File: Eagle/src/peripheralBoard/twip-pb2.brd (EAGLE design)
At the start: 110.2 x 69.8 mm, 31 parts, among them J1 UJ2-BH-1-TH, Q2 IRFD9120

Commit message: Update twip-pb2.brd
 mosfet pullup changes
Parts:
- moved R1 2.54 mm to (30.5, 73.7), turned to 285 degrees
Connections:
- net N$26: now also R1.2; no longer R1.1
- net N$7: now also R1.1; no longer R1.2
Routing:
- net N$8: track 137.1 -> 135.8 mm
- net N$26: track 24.2 -> 25.3 mm
- net N$11: track 28.9 -> 27.9 mm
- net N$18: track 29.1 -> 28.4 mm
- net N$19: track 29.4 -> 28.8 mm

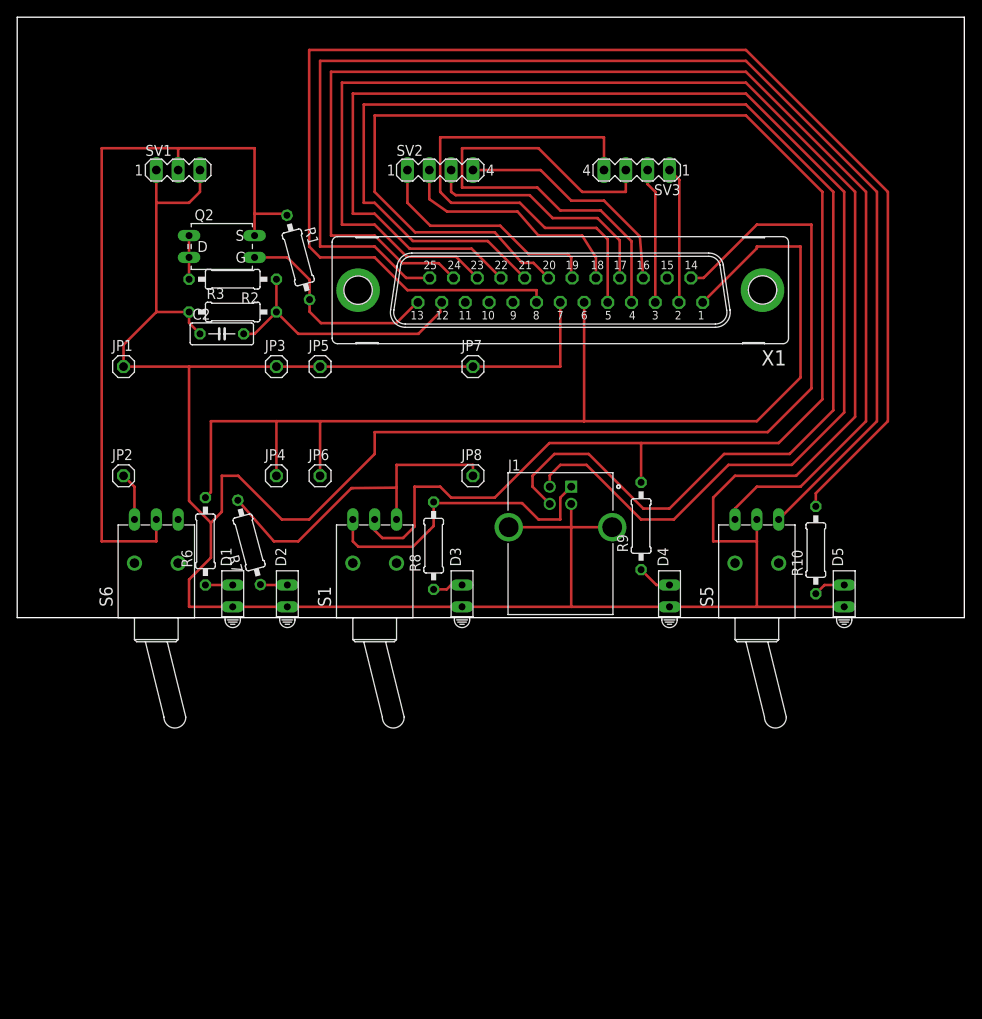
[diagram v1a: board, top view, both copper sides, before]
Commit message: Update twip-pb2.brd
big changes to  IBC pinouts  to  shift stepper connectors around
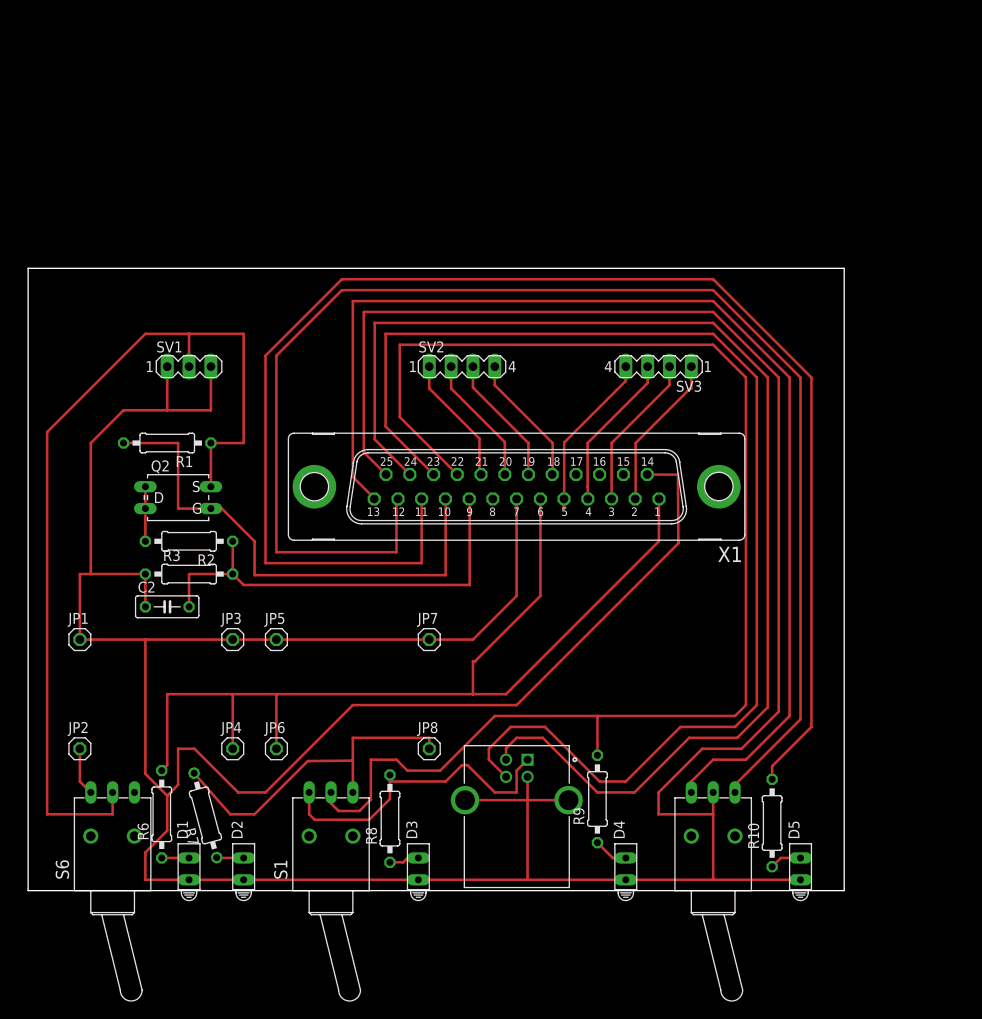
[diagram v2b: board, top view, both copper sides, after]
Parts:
- moved C2 32.4 mm to (15.2, 33.0)
- moved R10 32.2 mm to (85.6, 7.87)
- moved D1 32.2 mm to (17.8, 2.54)
- moved D2 32.2 mm to (24.1, 2.54)
- moved D3 32.2 mm to (44.5, 2.54)
- moved D4 32.2 mm to (68.6, 2.54)
- moved D5 32.2 mm to (88.9, 2.54)
- moved J1 32.2 mm to (57.1, 15.2)
- moved JP1 32.2 mm to (5.08, 29.2)
- moved JP2 32.2 mm to (5.08, 16.5)
- moved JP3 32.2 mm to (22.9, 29.2)
- moved JP4 32.2 mm to (22.9, 16.5)
- moved JP5 32.2 mm to (27.9, 29.2)
- moved JP6 32.2 mm to (27.9, 16.5)
- moved JP7 32.2 mm to (45.7, 29.2)
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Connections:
- net N$11: now also X1.21; no longer X1.19
- net N$12: now also X1.12; no longer X1.25
- net N$18: now also X1.20; no longer X1.18
- net N$19: now also X1.19; no longer X1.17
- net N$20: now also X1.18; no longer X1.16
- net N$21: now also X1.11; no longer X1.8
- net N$22: now also X1.24; no longer X1.22
- net N$23: now also X1.23; no longer X1.21
- net N$24: now also X1.22; no longer X1.20
- net N$26: now also X1.10; no longer X1.13
- net N$28: now also X1.13; no longer X1.24
- net N$29: now also X1.9; no longer X1.12
- net N$4: now also X1.25; no longer X1.23
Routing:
- net N$16: track 57.7 -> 18.3 mm
- net N$17: track 58.3 -> 20.6 mm
- net N$26: track 25.3 -> 59.5 mm
- net N$4: track 514.8 -> 491.4 mm
- net N$24: track 182.0 -> 161.1 mm
- net N$23: track 165.5 -> 144.7 mm
- net N$22: track 165.7 -> 145.0 mm
- net N$29: track 31.0 -> 50.8 mm
- net N$7: track 88.9 -> 107.6 mm
- net N$8: track 135.8 -> 117.4 mm
- net N$28: track 150.7 -> 134.0 mm
- net N$19: track 28.8 -> 15.2 mm
- net N$18: track 28.4 -> 15.1 mm
- net N$12: track 149.8 -> 162.8 mm
- net N$11: track 27.9 -> 15.0 mm
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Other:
- board size 110.2 x 69.8 mm -> 94.9 x 72.4 mm
